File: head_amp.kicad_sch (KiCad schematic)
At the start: 23 parts, among them J1 Conn_01x15, J2 Conn_01x15, J3 Conn_01x03, J4 Conn_01x03, J5 Left_Speaker, J6 Left_Mic, J7 Right_Speaker, J8 Right_Mic, M1 Fan, Q1 AO3401A, Q2 AO3400A, U1 LSM6DS3, U2 PJ-320A

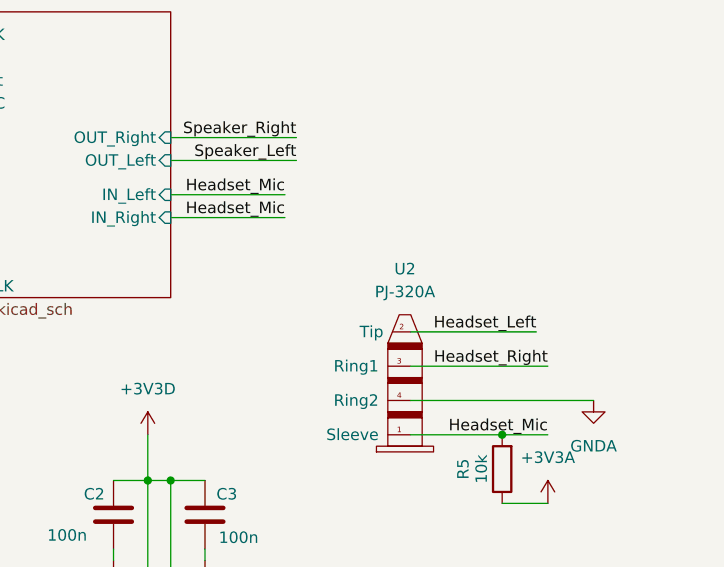
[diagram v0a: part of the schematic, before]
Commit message: Remove conflict silkscreen
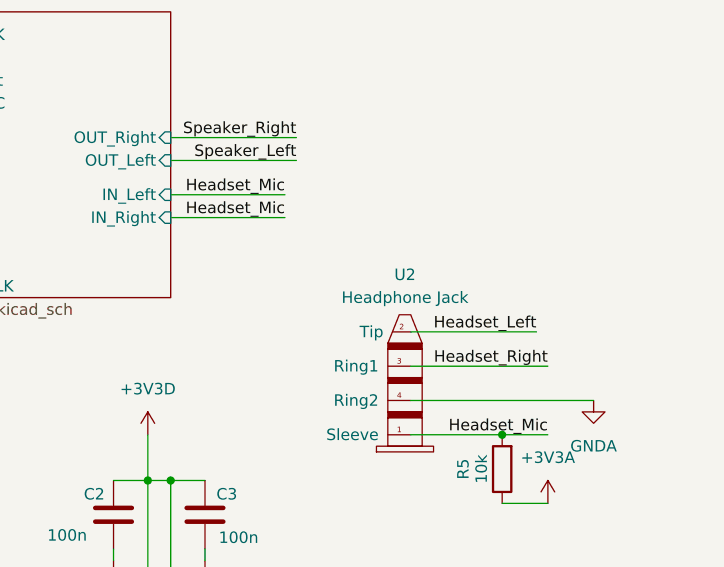
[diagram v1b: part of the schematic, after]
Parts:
- U2: value PJ-320A -> Headphone Jack
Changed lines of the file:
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@@
 		(fields_autoplaced yes)
 		(property "Reference" "U2"
-			(at 253.365 90.805 0)
+			(at 253.365 91.44 0)
 			(effects
 				(font
@@
 			)
 		)
-		(property "Value" "PJ-320A"
-			(at 253.365 93.345 0)
+		(property "Value" "Headphone Jack"
+			(at 253.365 93.98 0)
 			(effects
 				(font

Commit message: feat: pretty much done
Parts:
- removed C2, C3: 100n, Capacitor_SMD:C_0603_1608Metric, symbol Device:C
- removed J3: Conn_01x03, Connector_JST:JST_XH_S3B-XH-A_1x03_P2.50mm_Horizontal, symbol Connector_Generic:Conn_01x03
- removed U1: LSM6DS3, Package_LGA:LGA-14_3x2.5mm_P0.5mm_LayoutBorder3x4y, symbol Sensor_Motion:LSM6DS3
- added H1, H2, H3, H4: MountingHole, MountingHole:MountingHole_2.2mm_M2, symbol Mechanical:MountingHole
- added J3: Conn_01x05, Connector_JST:JST_XH_S5B-XH-A_1x05_P2.50mm_Horizontal, symbol Connector_Generic:Conn_01x05
- NT1, NT2: footprint (none) -> NetTie:NetTie-2_THT_Pad1.0mm
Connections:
- net +3V3D: now also J3.2 (Pin_2)
- net +5V: now also J4.1 (Pin_1), J3.1 (Pin_1)
- net Exit->Int_Select: now also J1.5 (Pin_5)
- net Ext->Int_CLK: now also J1.6 (Pin_6)
- net Ext->Int_In: now also J1.7 (Pin_7)
- net Ext->Int_LRC: now also J1.8 (Pin_8)
- net Ext->Int_Out: now also J1.9 (Pin_9)
- net GND: now also J4.3 (Pin_3), J3.5 (Pin_5)
- net Int->Ext_CLK: now also J2.8 (Pin_8)
- net Int->Ext_In: now also J2.7 (Pin_7)
- net Int->Ext_LRC: now also J2.6 (Pin_6)
- net Int->Ext_Out: now also J2.5 (Pin_5)
- net Int->Ext_Select: now also J2.9 (Pin_9)
- net MOSI: now also J1.10 (Pin_10)
- net SPI_CLK: now also J1.11 (Pin_11)
- net Master_Audio_Clk: now reaches J1.12 (Pin_12)
- net LED_Data: now reaches J1.4 (Pin_4)
- net LED_Data: now also J4.2 (Pin_2)
- net Out_DAT: now reaches J2.3 (Pin_3)
- net Out_DAT: now also J3.4 (Pin_4)
- net Out_CLK: now reaches J2.4 (Pin_4)
- net Out_CLK: now also J3.3 (Pin_3)
- no-connect marks 2 -> 0
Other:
- moved on the sheet: J4, NT1, NT2

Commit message: silkscreen
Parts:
- J1, J2: now left out of the parts list
- J3: footprint Connector_JST:JST_XH_S5B-XH-A_1x05_P2.50mm_Horizontal -> Connector_JST:JST_EH_S5B-EH_1x05_P2.50mm_Horizontal; LCSC (none) -> C265103
- J4: footprint Connector_JST:JST_XH_S3B-XH-A_1x03_P2.50mm_Horizontal -> Connector_JST:JST_EH_S3B-EH_1x03_P2.50mm_Horizontal; LCSC (none) -> C263754
- J5: footprint Connector_JST:JST_XH_S2B-XH-A_1x02_P2.50mm_Horizontal -> Connector_JST:JST_EH_S2B-EH_1x02_P2.50mm_Horizontal; LCSC C157931 -> C514173
- J6: value Left_Mic -> Left_Speaker; footprint Connector_JST:JST_XH_S2B-XH-A_1x02_P2.50mm_Horizontal -> Connector_JST:JST_EH_S2B-EH_1x02_P2.50mm_Horizontal; LCSC C157931 -> C514173
- J7: value Right_Speaker -> Left_Speaker; footprint Connector_JST:JST_XH_S2B-XH-A_1x02_P2.50mm_Horizontal -> Connector_JST:JST_EH_S2B-EH_1x02_P2.50mm_Horizontal; LCSC C157931 -> C514173
- J8: value Right_Mic -> Left_Speaker; footprint Connector_JST:JST_XH_S2B-XH-A_1x02_P2.50mm_Horizontal -> Connector_JST:JST_EH_S2B-EH_1x02_P2.50mm_Horizontal; LCSC C157931 -> C514173
- R1: value 50k -> 51k
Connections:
- net Out_CLK: now also J3.4 (Pin_4); no longer J3.3 (Pin_3)
- net Out_DAT: now also J3.3 (Pin_3); no longer J3.4 (Pin_4)
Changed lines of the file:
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@@
 		)
 	)
+	(label "Out_CLK"
+		(at 77.47 168.91 0)
+		(effects
+			(font
+				(size 1.27 1.27)
+			)
+			(justify left bottom)
+		)
+	)
 	(label "Ext->Int_CLK"
 		(at 62.23 74.93 0)
@@
 		)
 	)
-	(label "Out_CLK"
-		(at 77.47 166.37 0)
-		(effects
-			(font
-				(size 1.27 1.27)
-			)
-			(justify left bottom)
-		)
-	)
 	(label "Mic_Right"
 		(at 237.49 85.09 180)
@@
 		)
 	)
-	(label "Out_DAT"
-		(at 77.47 168.91 0)
-		(effects
-			(font
-				(size 1.27 1.27)
-			)
-			(justify left bottom)
-		)
-	)
 	(label "Int->Ext_Select"
 		(at 130.81 82.55 180)
@@
 		)
 	)
+	(label "Out_DAT"
+		(at 77.47 166.37 0)
+		(effects
+			(font
+				(size 1.27 1.27)
+			)
+			(justify left bottom)
+		)
+	)
 	(label "Headset_Right"
 		(at 242.57 76.2 180)
@@
 		(unit 1)
 		(exclude_from_sim no)
-		(in_bom yes)
+		(in_bom no)
 		(on_board yes)
 		(dnp no)
@@
 			)
 		)
-		(property "Value" "Right_Speaker"
+		(property "Value" "Left_Speaker"
 			(at 270.51 24.1299 0)
 			(effects
@@
 			)
 		)
-		(property "Footprint" "Connector_JST:JST_XH_S2B-XH-A_1x02_P2.50mm_Horizontal"
+		(property "Footprint" "Connector_JST:JST_EH_S2B-EH_1x02_P2.50mm_Horizontal"
 			(at 267.97 21.59 0)
 			(effects
@@
 			)
 		)
-		(property "LCSC" "C157931"
+		(property "LCSC" "C514173"
 			(at 267.97 21.59 0)
 			(effects
@@
 	)
 	(symbol
-		(lib_id "Connector_Generic:Conn_01x02")
-		(at 252.73 50.8 0)
-		(mirror y)
-		(unit 1)
-		(exclude_from_sim no)
-		(in_bom yes)
-		(on_board yes)
-		(dnp no)
-		(property "Reference" "J6"
-			(at 250.19 50.7999 0)
-			(effects
-				(font
-					(size 1.27 1.27)
-				)
-				(justify left)
-			)
-		)
-		(property "Value" "Left_Mic"
-			(at 250.19 53.3399 0)
-			(effects
-				(font
-					(size 1.27 1.27)
-				)
-				(justify left)
-			)
-		)
-		(property "Footprint" "Connector_JST:JST_XH_S2B-XH-A_1x02_P2.50mm_Horizontal"
-			(at 252.73 50.8 0)
-			(effects
-				(font
-					(size 1.27 1.27)
-				)
-				(hide yes)
-			)
-		)
-		(property "Datasheet" "~"
-			(at 252.73 50.8 0)
-			(effects
-				(font
-					(size 1.27 1.27)
-				)
-				(hide yes)
-			)
-		)
-		(property "Description" "Generic connector, single row, 01x02, script generated (kicad-library-utils/schlib/autogen/connector/)"
-			(at 252.73 50.8 0)
-			(effects
-				(font
-					(size 1.27 1.27)
-				)
-				(hide yes)
-			)
-		)
-		(property "LCSC" "C157931"
-			(at 252.73 50.8 0)
-			(effects
-				(font
-					(size 1.27 1.27)
-				)
-				(hide yes)
-			)
-		)
-		(pin "2"
-		)
-		(pin "1"
-		)
-		(instances
-			(project ""
-				(path "/0014c904-68b6-48b8-8ea7-8965ecf006e4"
-					(reference "J6")
-					(unit 1)
-				)
-			)
-		)
-	)
-	(symbol
 		(lib_id "power:+3V3")
 		(at 80.01 163.83 0)
@@
 	)
 	(symbol
+		(lib_id "Connector_Generic:Conn_01x02")
+		(at 267.97 50.8 0)
+		(unit 1)
+		(exclude_from_sim no)
+		(in_bom yes)
+		(on_board yes)
+		(dnp no)
+		(property "Reference" "J8"
+			(at 270.51 50.7999 0)
+			(effects
+				(font
+					(size 1.27 1.27)
+				)
+				(justify left)
+			)
+		)
+		(property "Value" "Left_Speaker"
+			(at 270.51 53.3399 0)
+			(effects
+				(font
+					(size 1.27 1.27)
+				)
+				(justify left)
+			)
+		)
+		(property "Footprint" "Connector_JST:JST_EH_S2B-EH_1x02_P2.50mm_Horizontal"
+			(at 267.97 50.8 0)
+			(effects
+				(font
+					(size 1.27 1.27)
+				)
+				(hide yes)
+			)
+		)
+		(property "Datasheet" "~"
+			(at 267.97 50.8 0)
+			(effects
+				(font
+					(size 1.27 1.27)
+				)
+				(hide yes)
+			)
+		)
+		(property "Description" "Generic connector, single row, 01x02, script generated (kicad-library-utils/schlib/autogen/connector/)"
+			(at 267.97 50.8 0)
+			(effects
+				(font
+					(size 1.27 1.27)
+				)
+				(hide yes)
+			)
+		)
+		(property "LCSC" "C514173"
+			(at 267.97 50.8 0)
+			(effects
+				(font
+					(size 1.27 1.27)
+				)
+				(hide yes)
+			)
+		)
+		(pin "2"
+		)
+		(pin "1"
+		)
+		(instances
+			(project "head_amp"
+				(path "/0014c904-68b6-48b8-8ea7-8965ecf006e4"
+					(reference "J8")
+					(unit 1)
+				)
+			)
+		)
+	)
+	(symbol
 		(lib_id "power:+5V")
 		(at 67.31 97.79 0)
@@
 			)
 		)
-		(property "Value" "50k"
+		(property "Value" "51k"
 			(at 123.19 139.954 90)
 			(effects
@@
 	)
 	(symbol
-		(lib_id "Connector_Generic:Conn_01x02")
-		(at 267.97 50.8 0)
-		(unit 1)
-		(exclude_from_sim no)
-		(in_bom yes)
-		(on_board yes)
-		(dnp no)
-		(property "Reference" "J8"
-			(at 270.51 50.7999 0)
-			(effects
-				(font
-					(size 1.27 1.27)
-				)
-				(justify left)
-			)
-		)
-		(property "Value" "Right_Mic"
-			(at 270.51 53.3399 0)
-			(effects
-				(font
-					(size 1.27 1.27)
-				)
-				(justify left)
-			)
-		)
-		(property "Footprint" "Connector_JST:JST_XH_S2B-XH-A_1x02_P2.50mm_Horizontal"
-			(at 267.97 50.8 0)
-			(effects
-				(font
-					(size 1.27 1.27)
-				)
-				(hide yes)
-			)
-		)
-		(property "Datasheet" "~"
-			(at 267.97 50.8 0)
-			(effects
-				(font
-					(size 1.27 1.27)
-				)
-				(hide yes)
-			)
-		)
-		(property "Description" "Generic connector, single row, 01x02, script generated (kicad-library-utils/schlib/autogen/connector/)"
-			(at 267.97 50.8 0)
-			(effects
-				(font
-					(size 1.27 1.27)
-				)
-				(hide yes)
-			)
-		)
-		(property "LCSC" "C157931"
-			(at 267.97 50.8 0)
-			(effects
-				(font
-					(size 1.27 1.27)
-				)
-				(hide yes)
-			)
-		)
-		(pin "2"
-		)
-		(pin "1"
-		)
-		(instances
-			(project "head_amp"
-				(path "/0014c904-68b6-48b8-8ea7-8965ecf006e4"
-					(reference "J8")
-					(unit 1)
-				)
-			)
-		)
-	)
-	(symbol
 		(lib_id "Transistor_FET:AO3400A")
 		(at 142.24 154.94 90)
@@
 			)
 		)
-		(property "Footprint" "Connector_JST:JST_XH_S2B-XH-A_1x02_P2.50mm_Horizontal"
+		(property "Footprint" "Connector_JST:JST_EH_S2B-EH_1x02_P2.50mm_Horizontal"
 			(at 252.73 21.59 0)
 			(effects
@@
 			)
 		)
-		(property "LCSC" "C157931"
+		(property "LCSC" "C514173"
 			(at 252.73 21.59 0)
 			(effects
@@
 		(unit 1)
 		(exclude_from_sim no)
-		(in_bom yes)
+		(in_bom no)
 		(on_board yes)
 		(dnp no)
@@
 	)
 	(symbol
+		(lib_id "Connector_Generic:Conn_01x02")
+		(at 252.73 50.8 0)
+		(mirror y)
+		(unit 1)
+		(exclude_from_sim no)
+		(in_bom yes)
+		(on_board yes)
+		(dnp no)
+		(property "Reference" "J6"
+			(at 250.19 50.7999 0)
+			(effects
+				(font
+					(size 1.27 1.27)
+				)
+				(justify left)
+			)
+		)
+		(property "Value" "Left_Speaker"
+			(at 250.19 53.3399 0)
+			(effects
+				(font
+					(size 1.27 1.27)
+				)
+				(justify left)
+			)
+		)
+		(property "Footprint" "Connector_JST:JST_EH_S2B-EH_1x02_P2.50mm_Horizontal"
+			(at 252.73 50.8 0)
+			(effects
+				(font
+					(size 1.27 1.27)
+				)
+				(hide yes)
+			)
+		)
+		(property "Datasheet" "~"
+			(at 252.73 50.8 0)
+			(effects
+				(font
+					(size 1.27 1.27)
+				)
+				(hide yes)
+			)
+		)
+		(property "Description" "Generic connector, single row, 01x02, script generated (kicad-library-utils/schlib/autogen/connector/)"
+			(at 252.73 50.8 0)
+			(effects
+				(font
+					(size 1.27 1.27)
+				)
+				(hide yes)
+			)
+		)
+		(property "LCSC" "C514173"
+			(at 252.73 50.8 0)
+			(effects
+				(font
+					(size 1.27 1.27)
+				)
+				(hide yes)
+			)
+		)
+		(pin "2"
+		)
+		(pin "1"
+		)
+		(instances
+			(project "head_amp"
+				(path "/0014c904-68b6-48b8-8ea7-8965ecf006e4"
+					(reference "J6")
+					(unit 1)
+				)
+			)
+		)
+	)
+	(symbol
 		(lib_id "Device:NetTie_2")
 		(at 74.93 113.03 0)
@@
 			)
 		)
-		(property "Footprint" "Connector_JST:JST_XH_S3B-XH-A_1x03_P2.50mm_Horizontal"
+		(property "Footprint" "Connector_JST:JST_EH_S3B-EH_1x03_P2.50mm_Horizontal"
 			(at 90.17 139.7 0)
 			(effects
@@
 			)
 		)
+		(property "LCSC" "C263754"
+			(at 90.17 139.7 0)
+			(effects
+				(font
+					(size 1.27 1.27)
+				)
+				(hide yes)
+			)
+		)
 		(pin "1"
 		)
@@
 			)
 		)
-		(property "Footprint" "Connector_JST:JST_XH_S5B-XH-A_1x05_P2.50mm_Horizontal"
+		(property "Footprint" "Connector_JST:JST_EH_S5B-EH_1x05_P2.50mm_Horizontal"
 			(at 90.17 166.37 0)
 			(effects
@@
 			(at 90.17 166.37 0)
 			(effects
+				(font
+					(size 1.27 1.27)
+				)
+				(hide yes)
+			)
+		)
+		(property "LCSC" "C265103"
+			(at 90.17 166.37 0)
+			(effects

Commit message: feat: overhaul
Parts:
- removed H2, H3, H4: MountingHole, MountingHole:MountingHole_2.2mm_M2, symbol Mechanical:MountingHole
- removed J1, J2: Conn_01x15, Connector_PinHeader_2.54mm:PinHeader_1x15_P2.54mm_Vertical, symbol Connector_Generic:Conn_01x15
- removed M1: Fan, A2543WR-4P:MOLEX_22053041, symbol Motor:Fan_Tacho_PWM
- removed NT1: NetTie_2, NetTie:NetTie-2_THT_Pad1.0mm, symbol Device:NetTie_2
- removed Q1: AO3401A, Package_TO_SOT_SMD:SOT-23, symbol Transistor_FET:AO3401A
- removed Q2: AO3400A, Package_TO_SOT_SMD:SOT-23, symbol Transistor_FET:AO3400A
- added C10: 1u, Capacitor_SMD:C_0603_1608Metric, symbol Device:C
- added C2, C38, C4, C9: 100n, Capacitor_SMD:C_0603_1608Metric, symbol Device:C
- added C3, C40: 22u, Capacitor_SMD:C_0603_1608Metric, symbol Device:C
- added C39: 10u, Capacitor_SMD:C_0603_1608Metric, symbol Device:C
- added C5, C6, C7, C8: 100n, Capacitor_SMD:C_0402_1005Metric, symbol Device:C
- added J1: USB Port, Connector_USB:USB_C_Receptacle_GCT_USB4105-xx-A_16P_TopMnt_Horizontal, symbol Connector:USB_C_Receptacle_USB2.0_16P
- added J8: Fan, Connector_JST:JST_EH_S2B-EH_1x02_P2.50mm_Horizontal, symbol Connector_Generic:Conn_01x02
- added Q1, Q2: MMBT3904, Package_TO_SOT_SMD:SOT-23, symbol Transistor_BJT:MMBT3904
- added Q3: AO3401A, Package_TO_SOT_SMD:SOT-23, symbol Transistor_FET:AO3401A
- added Q4: AO3400A, Package_TO_SOT_SMD:SOT-23, symbol Transistor_FET:AO3400A
- added R13, R14, R5, R6: 10k, Resistor_SMD:R_0402_1005Metric, symbol Device:R
- added R3, R4: 5.1k, Resistor_SMD:R_0402_1005Metric, symbol Device:R
- added SW1, SW2: SW_Push, Button_Switch_SMD:SW_SPST_TS-1088-xR020, symbol Switch:SW_Push
- added U1, U7: AMS1117-3.3, Package_TO_SOT_SMD:SOT-223-3_TabPin2, symbol Regulator_Linear:AMS1117-3.3
- added U2: CH340K, Package_SO:SSOP-10-1EP_3.9x4.9mm_P1mm_EP2.1x3.3mm, symbol Interface_USB:CH340K
- added U8: ESP32-WROOM-32E, RF_Module:ESP32-WROOM-32E, symbol RF_Module:ESP32-WROOM-32E
- C1: value 100n -> 10u; LCSC (none) -> C19702
- H1: footprint MountingHole:MountingHole_2.2mm_M2 -> MountingHole:MountingHole_3.2mm_M3
- J2: renamed from J3; value Conn_01x05 -> I2C
- J3: renamed from J4; value Conn_01x03 -> LED
- J4: renamed from J6; value Left_Speaker -> Left_Mic
- J6: renamed from J8; value Left_Speaker -> Right_Mic
- J7: value Left_Speaker -> Right_Speaker
- NT2: footprint NetTie:NetTie-2_THT_Pad1.0mm -> NetTie:NetTie-2_SMD_Pad2.0mm
- R1: value 51k -> 22; footprint Resistor_SMD:R_0603_1608Metric -> Resistor_SMD:R_0402_1005Metric; LCSC (none) -> C25092
- R10: renamed from R4; footprint Resistor_SMD:R_0603_1608Metric -> Resistor_SMD:R_0402_1005Metric; LCSC (none) -> C25744
- R2: value 27k -> 22; footprint Resistor_SMD:R_0603_1608Metric -> Resistor_SMD:R_0402_1005Metric; LCSC (none) -> C25092
- R8: renamed from R3; footprint Resistor_SMD:R_0603_1608Metric -> Resistor_SMD:R_0402_1005Metric; LCSC (none) -> C25744
- R9: renamed from R5; footprint Resistor_SMD:R_0603_1608Metric -> Resistor_SMD:R_0402_1005Metric; LCSC (none) -> C25744
- renumbered U2 to U4
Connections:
- net +3V3A: now also C40.2, U7.2 (VO)
- net +3V3D: now also C10.1, C3.2, C5.2, C9.2, R13.2, R14.2, U1.2 (VO), U2.7 (VCC), U8.2 (VDD)
- net +5V: now also C1.2, C2.1, C38.1, C39.2, C4.1, J1.A4 (VBUS), J1.A9 (VBUS), J1.B4 (VBUS), J1.B9 (VBUS), Q3.2 (S), U1.3 (VI), U7.3 (VI); no longer C1.1
- net Ext->Int_CLK: now also U8.27 (IO16)
- net Ext->Int_In: now also U8.28 (IO17)
- net Ext->Int_LRC: now also U8.29 (IO5)
- net Ext->Int_Out: now also U8.23 (IO15)
- net GND: now also C1.1, C10.2, C2.2, C3.1, C38.2, C39.1, C4.2, C40.1, C5.1, C6.2, C7.1, C8.1, C9.1, J1.A1 (GND), J1.A12 (GND), J1.B1 (GND), J1.B12 (GND), J1.S1 (SHIELD), J8.2 (Pin_2), Q4.2 (S), R3.2, R4.2, SW1.1, SW2.1, U1.1 (GND), U2.11 (GND), U2.3 (GND), U7.1 (GND), U8.1 (GND), U8.15 (GND), U8.38 (GND), U8.39 (GND); no longer C1.2, R1.1
- net Int->Ext_CLK: now also U8.16 (IO13)
- net Int->Ext_In: now also U8.12 (IO27)
- net Int->Ext_LRC: now also U8.13 (IO14)
- net Int->Ext_Out: now also U8.14 (IO12)
- net Int->Ext_Select: now also U8.6 (IO34)
- net LED_Data: now also U8.10 (IO25)
- net MOSI: now also U8.7 (IO35)
- net Out_CLK: now also U8.30 (IO18)
- net Out_DAT: now also U8.31 (IO19)
- net SPI_CLK: now also U8.8 (IO32)
- net USB_D+: now reaches R2.2
- net USB_D+: now also U2.1 (UD+)
- net FAN_RPM: no longer names the net of R2.1
- net FAN_RPM: now also J1.A6 (D+), J1.B6 (D+); no longer R1.2
- new net: J8.1 (Pin_1), Q3.3 (D), Q4.3 (D)
- new net: J1.A7 (D-), J1.B7 (D-), R1.1
- new net: Q2.1 (B), R6.2
- new net: J1.B5 (CC2), R4.1
- new net: Q1.1 (B), R5.2
- new net: J1.A5 (CC1), R3.1
- new net: C6.1, U2.10 (V3)
- new net DTR: Q2.2 (E), R5.1, U2.4 (~{DTR})
- new net Ext->Int_Select: U8.26 (IO4)
- new net Fan_PWM: Q3.1 (G), Q4.1 (G), U8.11 (IO26)
- new net GPIO0: C7.2, Q2.3 (C), R14.1, SW1.2, U8.25 (IO0)
- new net MCU_EN: C8.2, Q1.3 (C), R13.1, SW2.2, U8.3 (EN)
- new net Prog_RX: U2.8 (TXD), U8.34 (RXD0/IO3)
- new net Prog_TX: U2.9 (RXD), U8.35 (TXD0/IO1)
- new net RTS: Q1.2 (E), R6.1, U2.6 (~{RTS})
- new net USB_D-: R1.2, U2.2 (UD-)
- no-connect marks 0 -> 4
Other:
- note added: "I2S master clock can only come from GPIO0"
- moved on the sheet: H1, J2, J3, J4, J5, J6, J7, NT2, R10, R8, R9, U4

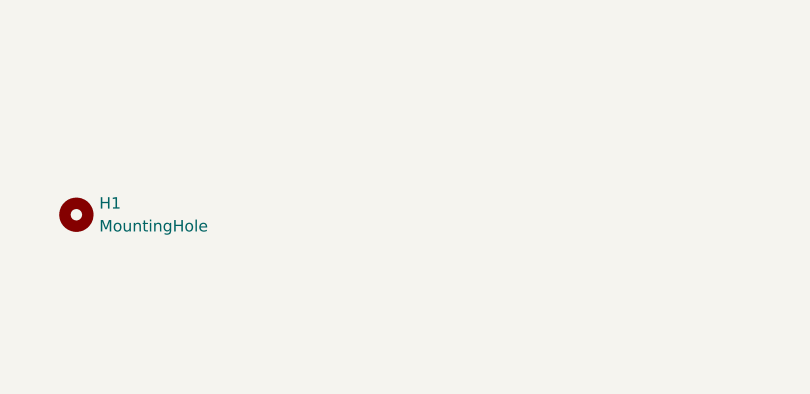
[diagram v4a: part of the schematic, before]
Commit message: add 3d models and tooling holes
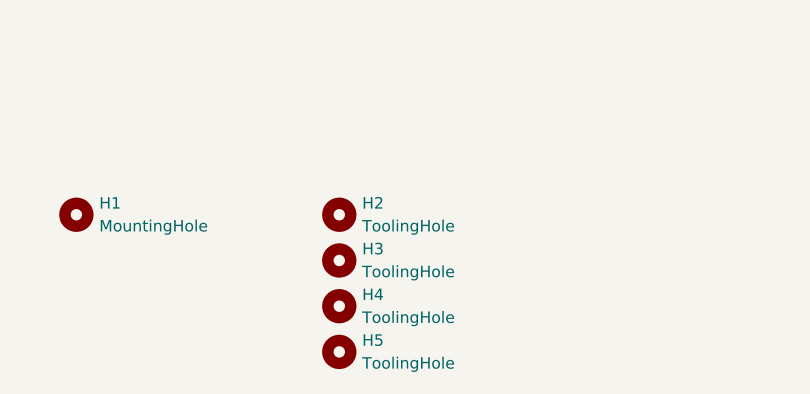
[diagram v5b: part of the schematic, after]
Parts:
- added H2, H3, H4, H5: ToolingHole, MountingHole:ToolingHole_1.152mm, symbol Mechanical:MountingHole

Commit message: compactify
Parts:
- added H6: MountingHole, MountingHole:MountingHole_3.2mm_M3, symbol Mechanical:MountingHole
- C4: footprint Capacitor_SMD:C_0603_1608Metric -> Capacitor_SMD:C_0402_1005Metric; LCSC C14663 -> C307331
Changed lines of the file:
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@@
 	)
 	(symbol
+		(lib_id "Mechanical:MountingHole")
+		(at 88.9 182.88 0)
+		(unit 1)
+		(exclude_from_sim no)
+		(in_bom no)
+		(on_board yes)
+		(dnp no)
+		(fields_autoplaced yes)
+		(property "Reference" "H6"
+			(at 91.44 181.6099 0)
+			(effects
+				(font
+					(size 1.27 1.27)
+				)
+				(justify left)
+			)
+		)
+		(property "Value" "MountingHole"
+			(at 91.44 184.1499 0)
+			(effects
+				(font
+					(size 1.27 1.27)
+				)
+				(justify left)
+			)
+		)
+		(property "Footprint" "MountingHole:MountingHole_3.2mm_M3"
+			(at 88.9 182.88 0)
+			(effects
+				(font
+					(size 1.27 1.27)
+				)
+				(hide yes)
+			)
+		)
+		(property "Datasheet" "~"
+			(at 88.9 182.88 0)
+			(effects
+				(font
+					(size 1.27 1.27)
+				)
+				(hide yes)
+			)
+		)
+		(property "Description" "Mounting Hole without connection"
+			(at 88.9 182.88 0)
+			(effects
+				(font
+					(size 1.27 1.27)
+				)
+				(hide yes)
+			)
+		)
+		(instances
+			(project "head_amp"
+				(path "/0014c904-68b6-48b8-8ea7-8965ecf006e4"
+					(reference "H6")
+					(unit 1)
+				)
+			)
+		)
+	)
+	(symbol
 		(lib_id "Device:C")
 		(at 80.01 25.4 90)
@@
 			)
 		)
-		(property "Footprint" "Capacitor_SMD:C_0603_1608Metric"
+		(property "Footprint" "Capacitor_SMD:C_0402_1005Metric"
 			(at 66.04 145.0848 0)
 			(effects
@@
 			)
 		)
-		(property "LCSC" "C14663"
+		(property "LCSC" "C307331"
 			(at 62.23 146.05 90)
 			(effects
